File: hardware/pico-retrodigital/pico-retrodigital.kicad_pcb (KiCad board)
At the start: 2 copper layers, 50 x 38 mm, 70 parts, among them J1 Conn_02x05_Top_Bottom, J3 Conn_01x14, J4 Conn_01x02_Pin, J5 USB_C_Plug_USB2.0, U1 SN74LVC1G17DBVR, U2 SN74LVC1G17DBVR, U3 RP2354B, U4 SN74LVC245APW, U5 SN74LVC245APW, U6 SN74LVC245APW, U8 ME6217C33M5G, Y1 ABM8-272-T3

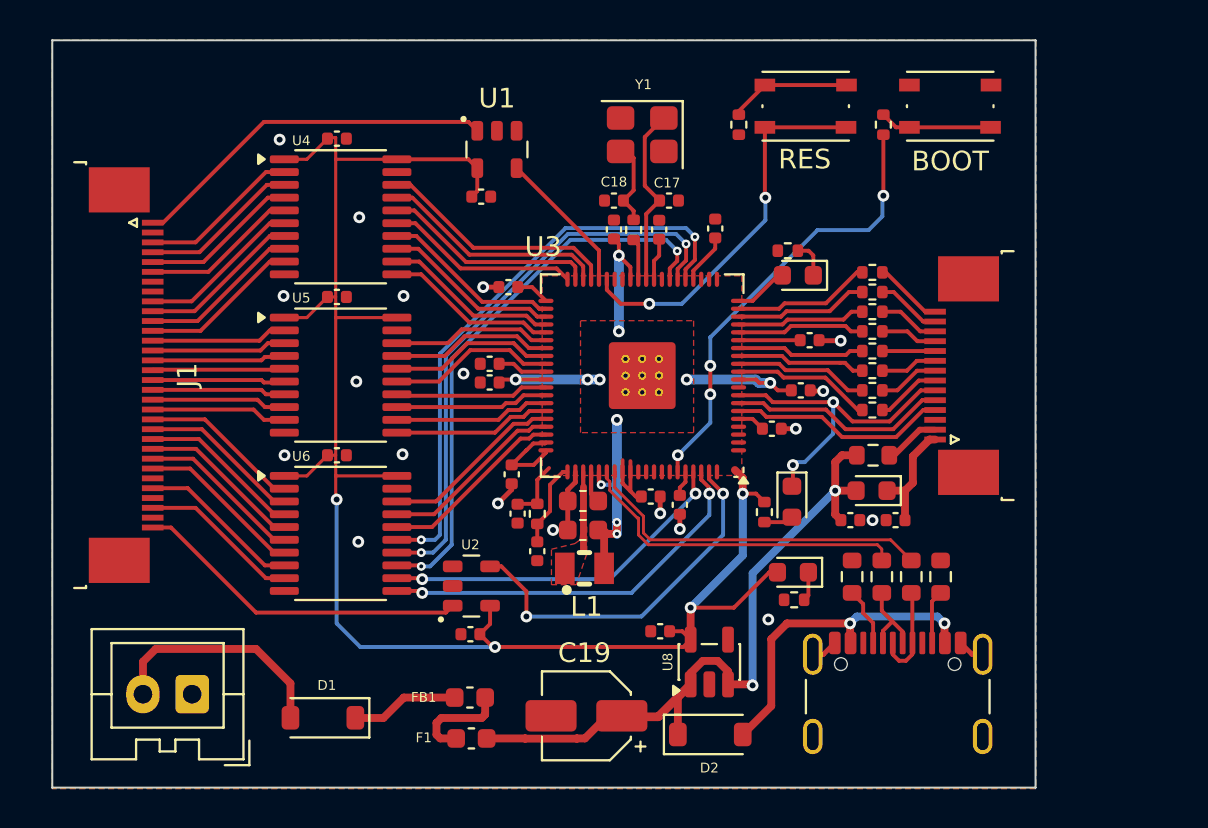
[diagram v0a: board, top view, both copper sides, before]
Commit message: Two HDMI out connectors
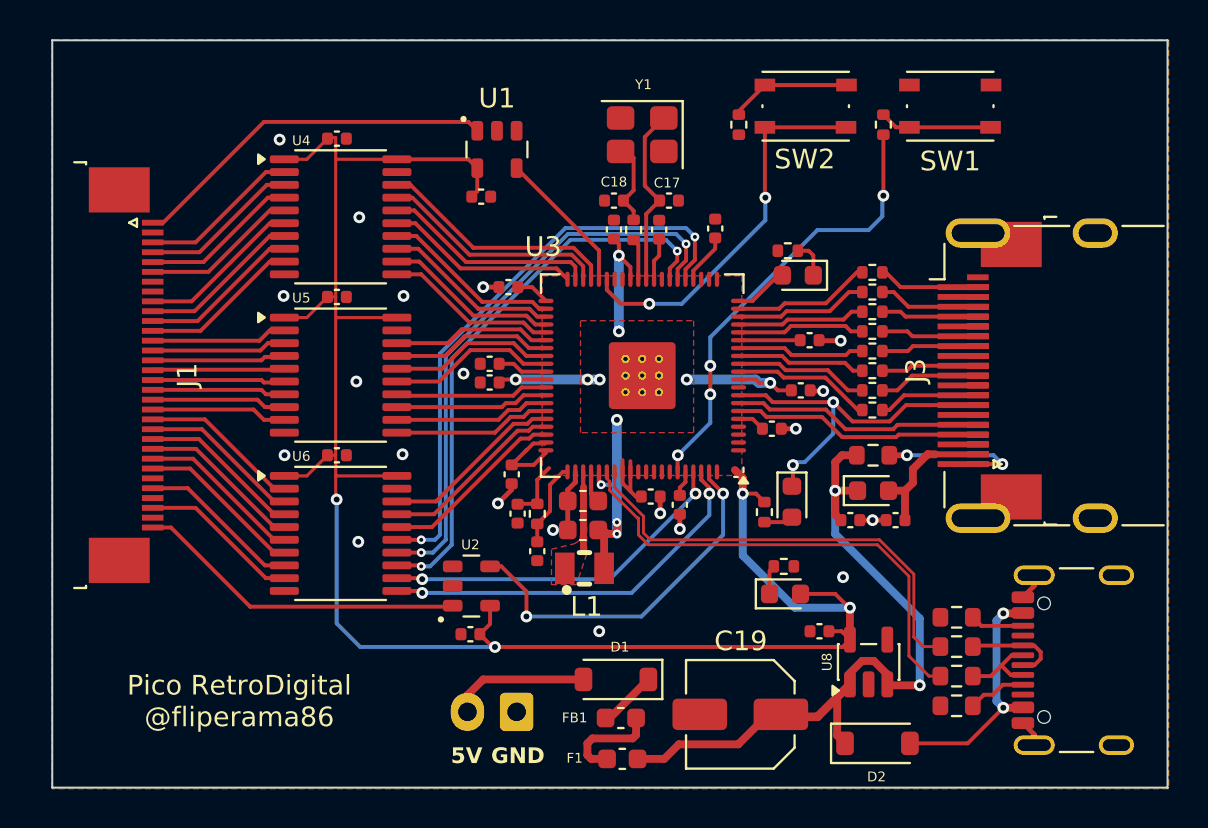
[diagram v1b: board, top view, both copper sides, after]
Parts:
- added J2: HDMI_A_1.4, Connector_Video:HDMI_A_Molex_208658-1001_Horizontal, F.Cu at (92.0, 92.5)
- C19: footprint Capacitor_SMD:CP_Elec_4x3 -> Capacitor_SMD:C_Elec_5x5.4
- J3: value Conn_01x14 -> 2-1734839-0; footprint Connector_FFC-FPC:TE_1-1734839-4_1x14-1MP_P0.5mm_Horizontal -> Connector_FFC-FPC:TE_2-1734839-0_1x20-1MP_P0.5mm_Horizontal
- moved J4 16.5 mm to (66.0, 109.6)
- moved D1 15.0 mm to (71.1, 108.0)
- moved J5 10.4 mm to (95.5, 107.0), turned to 90 degrees
- moved D2 8.51 mm to (84.4, 111.2)
- moved R18 8.45 mm to (88.4, 109.3), turned to 0 degrees
- moved C10 8.10 mm to (81.5, 105.5)
- moved U8 8.10 mm to (84.0, 107.1)
- moved C19 7.83 mm to (77.4, 109.7)
- moved F1 7.75 mm to (71.4, 112.0)
- moved FB1 7.75 mm to (71.3, 109.9)
- moved R17 6.33 mm to (88.4, 107.8), turned to 0 degrees
- moved R16 4.24 mm to (88.4, 106.3), turned to 0 degrees
- moved R19 2.22 mm to (88.4, 104.8), turned to 180 degrees
- moved J3 2.19 mm to (90.9, 92.2)
- moved R14 1.78 mm to (79.6, 102.2), turned to 0 degrees
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- renumbered BOOT to SW1, RES to SW2
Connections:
- C23 pad 1: Net-(D3-K) -> /HDMI5V
- D3 pad 1: Net-(D3-K) -> +5V
- D3 pad 2: +5V -> /HDMI5V
- J3 pad 1: Net-(D3-K) -> /HPD
- J3 pad 10: D0+ -> CLK+
- J3 pad 11: D1- -> D0-
- J3 pad 12: D1+ -> GND
- J3 pad 13: D2- -> D0+
- J3 pad 14: D2+ -> D1-
- J3 pad 2: Net-(J3-Pin_2) -> /HDMI5V
- J3 pad 6: CEC_PICO -> /UTILITY
- J3 pad 7: CLK- -> CEC_PICO
- J3 pad 8: CLK+ -> CLK-
- J3 pad 9: D0- -> GND
- J3 pad MP: (no net) -> GND
- R2 pad 2: Net-(J3-Pin_2) -> /HPD
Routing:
- net +3V3: track 115.8 -> 124.4 mm
- net USB_D-: track 17.1 -> 24.6 mm
- net /HPD: track 0.00 -> 7.18 mm, vias 0 -> 2
- net Net-(D3-K): track 5.81 -> 0.00 mm
- net USB_D+: track 17.9 -> 23.1 mm
- net /HDMI5V: track 0.00 -> 5.06 mm
- net +5V MVS: track 11.9 -> 7.36 mm
- net Net-(D2-A): track 16.9 -> 12.6 mm
- net Net-(J3-Pin_2): track 2.87 -> 0.00 mm
- net Net-(D1-K): track 5.48 -> 2.99 mm
- net +5V: track 36.2 -> 38.1 mm
- net D0+: track 2.68 -> 4.21 mm
- net GND: track 12.1 -> 13.4 mm, vias 19 -> 20
- net D1-: track 2.89 -> 4.21 mm
- net D0-: track 2.89 -> 4.21 mm
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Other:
- board size 50 x 38 mm -> 56.7 x 38 mm
- board text added: "5V"
- board text added: "GND"
- board text added: "Pico RetroDigital @fliperama86"

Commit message: Source everything from JLC: LCSC part fill, connector swaps, fab export fixes
- Fill LCSC/MPN fields across the BOM (fill_lcsc script + curated picks);
  replace generic values with specific parts (diodes, LEDs, polyfuse,
  ferrite bead, switches)
- C19: SMD electrolytic -> 47uF 1206 MLCC (keeps Economic assembly)
- J1/J3: TE 1734839 FFC -> LCSC-stocked double-sided-contact parts
  (AFC24-S32FIA-00 / Molex 5034802000), project-local footprints
- J5: GCT USB4105 -> HRO TYPE-C-31-M-12 (C165948)
- D3/D4: SS14 -> true 0603 Schottky (CD0603-B0340R)
- Fabrication Toolkit rotation offsets for J2/U3; J3/J4 DNP and
  excluded from BOM/CPL; remove duplicate C5 footprint
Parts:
- removed the C5 at (73.3, 85.1)
- C19: footprint Capacitor_SMD:C_Elec_5x5.4 -> Capacitor_SMD:C_1206_3216Metric
- D1, D2: value D_Schottky -> DSK14
- D3, D4: value SS14 -> CD0603-B0340R
- D5: value LED -> GREEN
- D6: value LED -> RED
- F1: value Polyfuse -> 500mA
- FB1: value FerriteBead -> 600R@100MHz
- J1: value Conn_02x05_Top_Bottom -> AFC24-S32FIA-00; footprint Connector_FFC-FPC:TE_3-1734839-2_1x32-1MP_P0.5mm_Horizontal -> pico-retrodigital:FPC-SMD_P0.50-32P_JS_AFC24-S32FIA-00
- J3: value 2-1734839-0 -> 5034802000; footprint Connector_FFC-FPC:TE_2-1734839-0_1x20-1MP_P0.5mm_Horizontal -> pico-retrodigital:FPC-SMD_5034802000
- J5: footprint Connector_USB:USB_C_Receptacle_GCT_USB4105-xx-A_16P_TopMnt_Horizontal -> pico-retrodigital:USB_C_Receptacle_HRO_TYPE-C-31-M-12
- SW1: value BOOT -> K2-1808SN-A4SW-01
- SW2: value RES -> K2-1808SN-A4SW-01
- moved J1 0.23 mm to (46.0, 92.5)
- moved C19 0.10 mm to (77.4, 109.8), turned to 90 degrees
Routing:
- net +3V3: track 124.4 -> 121.1 mm
- net Net-(D2-A): track 12.6 -> 11.9 mm
- net Net-(J5-D--PadA7): track 4.28 -> 4.85 mm

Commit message: Add SW3/SW4 user buttons on GPIO4/GPIO5; 4-layer board
- Two new pushbuttons (same K2-1808SN as BOOT/RES) with 1k series
  resistors to GND, routed on In1.Cu
- Board converted to 4 copper layers, JLC7628 1.6mm stackup documented;
  inner layers are plain signal layers
- USB-C J5: FT Position Offset 1.42mm (JLC part origin vs KiCad anchor,
  measured via shell-hole alignment against JLC's own footprint)
- Restore GPIO6 no-connect marker
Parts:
- added R21: 1k, Resistor_SMD:R_0402_1005Metric, F.Cu at (50.4, 107.4)
- added R22: 1k, Resistor_SMD:R_0402_1005Metric, F.Cu at (57.5, 107.4)
- added SW3: K2-1808SN-A4SW-01, Button_Switch_SMD:SW_Push_1P1T_NO_Vertical_Wuerth_434133025816, F.Cu at (48.5, 109.8)
- added SW4: K2-1808SN-A4SW-01, Button_Switch_SMD:SW_Push_1P1T_NO_Vertical_Wuerth_434133025816, F.Cu at (55.6, 109.8)
- moved J4 2.55 mm to (63.5, 109.6), turned to 0 degrees
- moved D4 0.70 mm to (80.8, 98.9)
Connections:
- U3 pad 1: unconnected-(U3-GPIO4-Pad1) -> Net-(U3-GPIO4)
- U3 pad 2: unconnected-(U3-GPIO5-Pad2) -> Net-(U3-GPIO5)
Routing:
- net Net-(U3-GPIO4): track 0.00 -> 42.1 mm, vias 0 -> 2
- net Net-(U3-GPIO5): track 0.00 -> 34.4 mm, vias 0 -> 2
- net Net-(R21-Pad2): track 0.00 -> 5.61 mm
- net Net-(R22-Pad2): track 0.00 -> 5.61 mm
- net +5V MVS: track 7.36 -> 4.42 mm
- net Net-(D4-A): track 1.50 -> 2.20 mm
- net CEC_PICO: track 17.7 -> 17.1 mm
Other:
- copper layers 2 -> 4

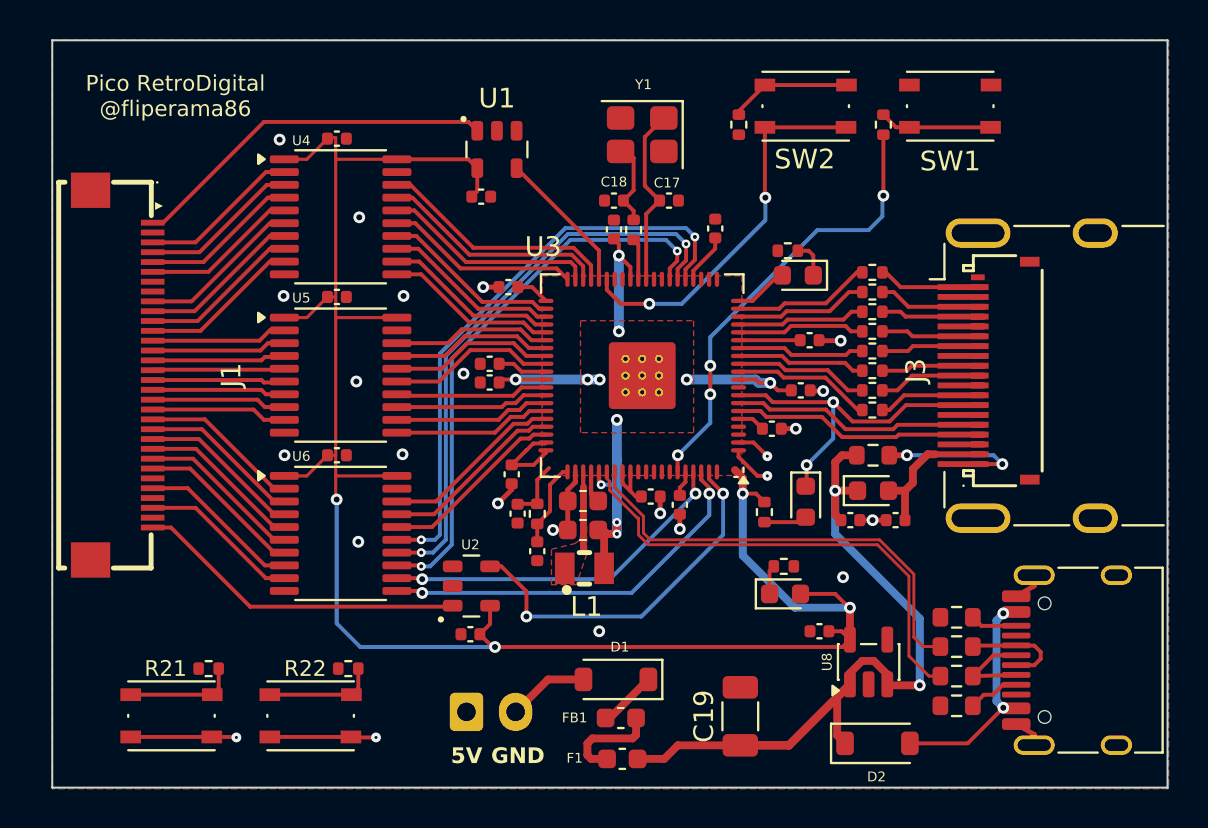
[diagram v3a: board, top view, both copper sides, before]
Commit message: Full JCLPCB parts filled
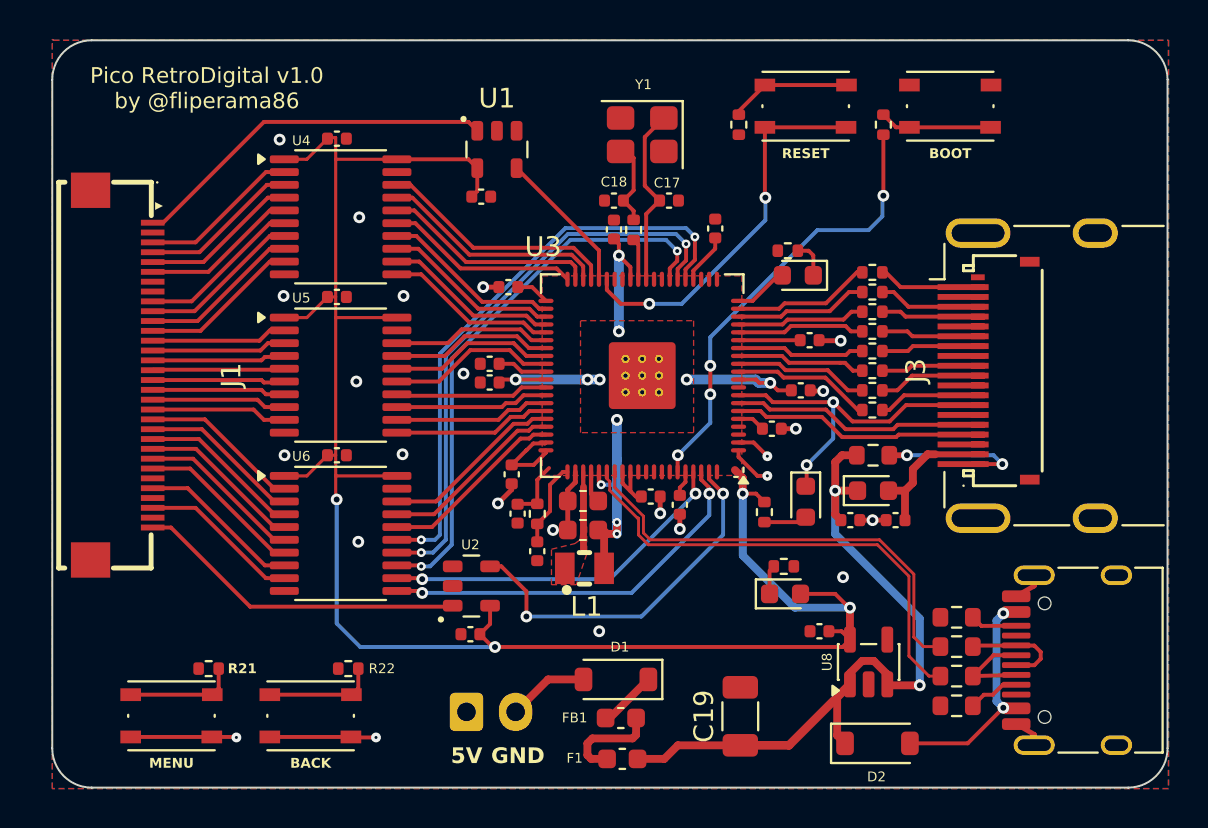
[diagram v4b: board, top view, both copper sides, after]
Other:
- outline, holes or cut-outs redrawn
- board text added: "BACK"
- board text added: "BOOT"
- board text added: "MENU"
- board text added: "Pico RetroDigital v1.0 by @fliperama86"
- board text added: "RESET"
- board text removed: "Pico RetroDigital @fliperama86"
